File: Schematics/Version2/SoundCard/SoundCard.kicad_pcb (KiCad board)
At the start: 6 copper layers, 101.6 x 38.4 mm, 46 parts, among them J1 Screw_Terminal_01x03, J2 AudioJack3, J3 Conn, Q1 Q_NJFET_DSG, Q2 Q_NJFET_DSG, Q3 Q_NJFET_DSG, Q4 Q_NJFET_DSG, U1 TL072, U2 MAX505, U3 AS3340, U4 TL072, U5 TL072

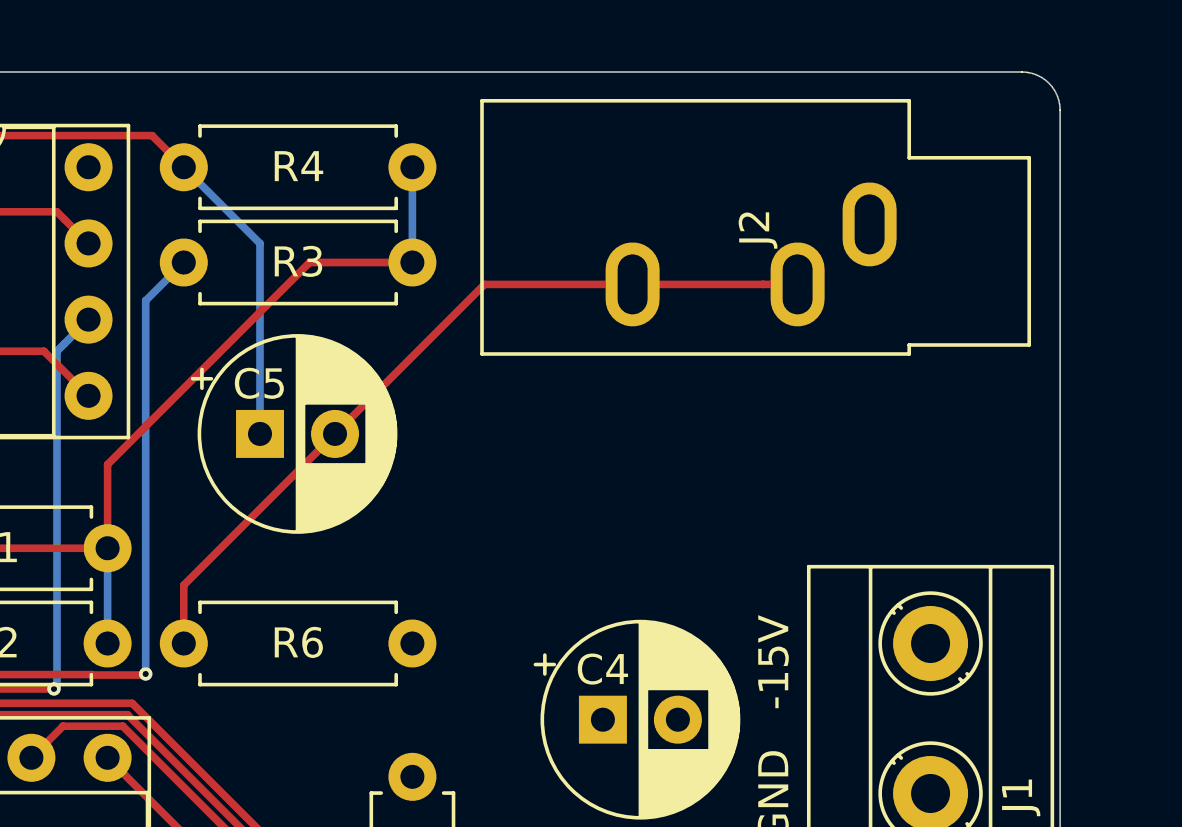
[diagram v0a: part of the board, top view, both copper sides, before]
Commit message: Update the footprint for the 3.5mm jack.
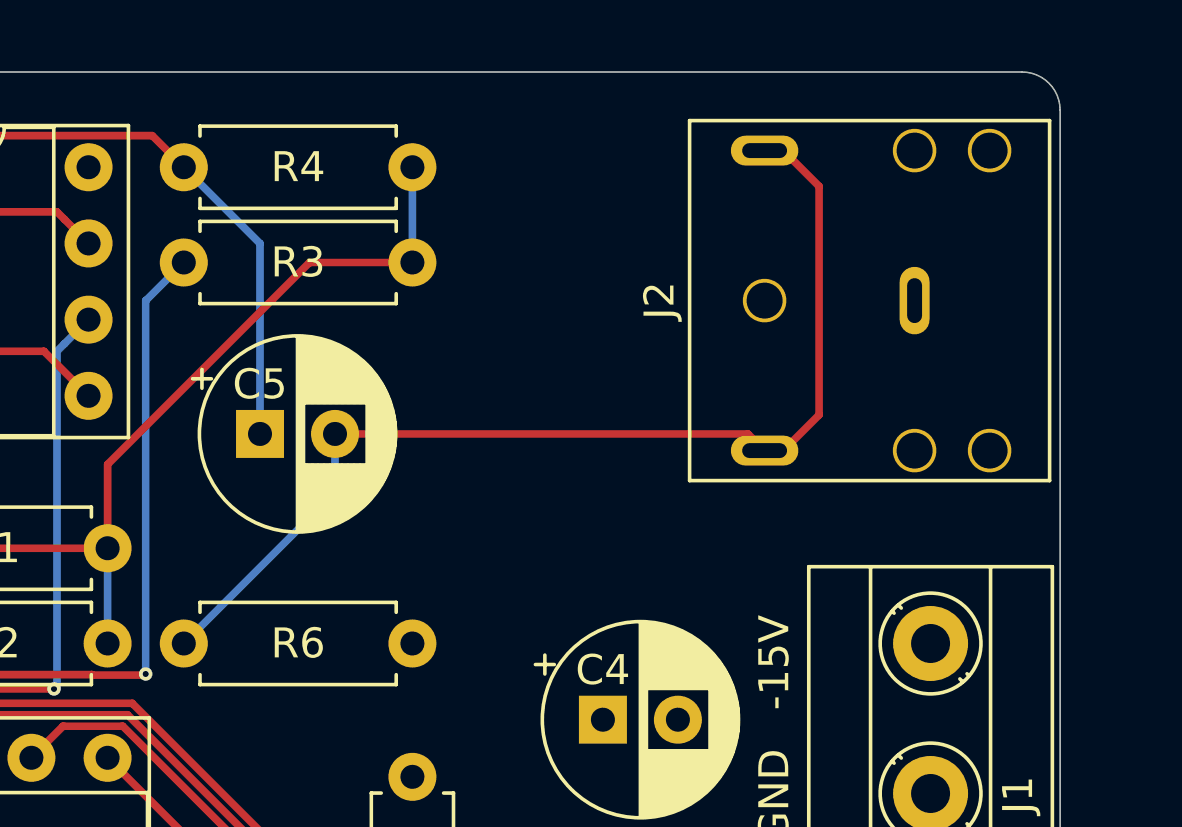
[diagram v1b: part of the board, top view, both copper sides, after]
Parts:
- J2: footprint Connector_Audio:Jack_3.5mm_CUI_SJ1-3533NG_Horizontal -> Connector_Audio:Jack_3.5mm_CUI_SJ1-3523N
- moved J2 2.54 mm to (158.8, 106.7)
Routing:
- net Net-(C5-Pad2): track 26.6 -> 35.9 mm
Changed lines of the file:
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@@
     (thickness 1.6)
     (drawings 11)
-    (tracks 297)
+    (tracks 300)
     (zones 0)
     (modules 46)
@@
     (add_net VCC)
   )
+  (module Connector_Audio:Jack_3.5mm_CUI_SJ1-3523N (layer F.Cu)
+    (at 158.75 106.68 270)
+    (fp_text reference J2 (at 0 7 270) (layer F.SilkS)
+      (effects (font (size 1 1) (thickness 0.15)))
+    )
+    (fp_text value AudioJack3 (at 0 8.5 270) (layer F.Fab)
+      (effects (font (size 1 1) (thickness 0.15)))
+    )
+    (fp_line (start -6 6) (end -6 -6) (layer F.SilkS) (width 0.12))
+    (fp_line (start 6 -6) (end 6 6) (layer F.SilkS) (width 0.12))
+    (fp_line (start -6 6) (end 6 6) (layer F.SilkS) (width 0.12))
+    (fp_line (start -6 -6) (end 6 -6) (layer F.SilkS) (width 0.12))
+    (pad "" thru_hole circle (at -5 -4) (size 1.45 1.45) (drill 1.2) (layers *.Cu *.Mask))
+    (pad "" thru_hole circle (at 5 -4) (size 1.45 1.45) (drill 1.2) (layers *.Cu *.Mask))
+    (pad "" thru_hole circle (at -5 -1.5) (size 1.45 1.45) (drill 1.2) (layers *.Cu *.Mask))
+    (pad "" thru_hole circle (at 5 -1.5) (size 1.45 1.45) (drill 1.2) (layers *.Cu *.Mask))
+    (pad "" thru_hole circle (at 0 3.5) (size 1.45 1.45) (drill 1.2) (layers *.Cu *.Mask))
+    (pad R thru_hole oval (at 5 3.5 270) (size 1 2.25) (drill oval 0.5 1.5) (layers *.Cu *.Mask)
+      (net 24 "Net-(C5-Pad2)"))
+    (pad T thru_hole oval (at -5 3.5 270) (size 1 2.25) (drill oval 0.5 1.5) (layers *.Cu *.Mask)
+      (net 24 "Net-(C5-Pad2)"))
+    (pad S thru_hole oval (at 0 -1.5) (size 1 2.25) (drill oval 0.5 1.5) (layers *.Cu *.Mask)
+      (net 23 GNDA))
+  )
   (module Connector_PinHeader_2.54mm:PinHeader_2x40_P2.54mm_Horizontal (layer F.Cu)
     (at 163.83 133.35 270)
@@
     )
   )
-  (module Connector_Audio:Jack_3.5mm_CUI_SJ1-3533NG_Horizontal (layer F.Cu)
-    (at 158.75 104.14 270)
-    (descr "TRS 3.5mm, horizontal, through-hole, https://www.cui.com/product/resource/sj1-353xng.pdf")
-    (tags "TRS audio jack stereo horizontal")
-    (fp_text reference J2 (at 0.1 3.81 270) (layer F.SilkS)
-      (effects (font (size 1 1) (thickness 0.15)))
-    )
-    (fp_text value AudioJack3 (at 0.1 14.05 270) (layer F.Fab)
-      (effects (font (size 1 1) (thickness 0.15)))
-    )
-    (fp_text user %R (at 0.1 3.8 270) (layer F.Fab)
-      (effects (font (size 1 1) (thickness 0.15)))
-    )
-    (fp_line (start 4.7 -5.7) (end -4.5 -5.7) (layer F.CrtYd) (width 0.05))
-    (fp_line (start 4.7 13.3) (end 4.7 -5.7) (layer F.CrtYd) (width 0.05))
-    (fp_line (start -4.5 13.3) (end 4.7 13.3) (layer F.CrtYd) (width 0.05))
-    (fp_line (start -4.5 -5.7) (end -4.5 13.3) (layer F.CrtYd) (width 0.05))
-    (fp_line (start -2.22 -1.32) (end -2.22 -5.32) (layer F.SilkS) (width 0.12))
-    (fp_line (start -4.12 -1.32) (end -2.22 -1.32) (layer F.SilkS) (width 0.12))
-    (fp_line (start -4.12 12.92) (end -4.12 -1.32) (layer F.SilkS) (width 0.12))
-    (fp_line (start 4.32 12.92) (end -4.12 12.92) (layer F.SilkS) (width 0.12))
-    (fp_line (start 4.32 -1.32) (end 4.32 12.92) (layer F.SilkS) (width 0.12))
-    (fp_line (start 4.02 -1.32) (end 4.32 -1.32) (layer F.SilkS) (width 0.12))
-    (fp_line (start 4.02 -5.32) (end 4.02 -1.32) (layer F.SilkS) (width 0.12))
-    (fp_line (start -2.22 -5.32) (end 4.02 -5.32) (layer F.SilkS) (width 0.12))
-    (fp_line (start -2.1 -1.2) (end -2.1 -5.2) (layer F.Fab) (width 0.1))
-    (fp_line (start -4 -1.2) (end -2.1 -1.2) (layer F.Fab) (width 0.1))
-    (fp_line (start -4 12.8) (end -4 -1.2) (layer F.Fab) (width 0.1))
-    (fp_line (start 4.2 12.8) (end -4 12.8) (layer F.Fab) (width 0.1))
-    (fp_line (start 4.2 -1.2) (end 4.2 12.8) (layer F.Fab) (width 0.1))
-    (fp_line (start 3.9 -1.2) (end 4.2 -1.2) (layer F.Fab) (width 0.1))
-    (fp_line (start 3.9 -5.2) (end 3.9 -1.2) (layer F.Fab) (width 0.1))
-    (fp_line (start -2.1 -5.2) (end 3.9 -5.2) (layer F.Fab) (width 0.1))
-    (pad R thru_hole oval (at 2 7.9 270) (size 2.8 1.8) (drill oval 2 1) (layers *.Cu *.Mask)
-      (net 24 "Net-(C5-Pad2)"))
-    (pad T thru_hole oval (at 2 2.4 270) (size 2.8 1.8) (drill oval 2 1) (layers *.Cu *.Mask)
-      (net 24 "Net-(C5-Pad2)"))
-    (pad S thru_hole oval (at 0 0 270) (size 2.8 1.8) (drill oval 2 1) (layers *.Cu *.Mask)
-      (net 23 GNDA))
-    (model ${KISYS3DMOD}/Connector_Audio.3dshapes/Jack_3.5mm_CUI_SJ1-3533NG_Horizontal.wrl
-      (at (xyz 0 0 0))
-      (scale (xyz 1 1 1))
-      (rotate (xyz 0 0 0))
-    )
-  )
   (module Capacitor_THT:CP_Radial_D6.3mm_P2.50mm (layer F.Cu)
     (at 149.86 120.65)
@@
   (segment (start 114.515999 125.945999) (end 117.310001 128.740001) (width 0.254) (layer B.Cu) (net 23))
   (segment (start 115.57 118.11) (end 114.515999 119.164001) (width 0.254) (layer B.Cu) (net 23))
-  (segment (start 155.196 106.14) (end 150.85 106.14) (width 0.254) (layer F.Cu) (net 24))
-  (segment (start 156.35 106.14) (end 155.196 106.14) (width 0.254) (layer F.Cu) (net 24))
-  (segment (start 145.915 106.14) (end 140.93 111.125) (width 0.254) (layer F.Cu) (net 24))
-  (segment (start 150.85 106.14) (end 145.915 106.14) (width 0.254) (layer F.Cu) (net 24))
-  (segment (start 135.89 116.165) (end 135.89 118.11) (width 0.254) (layer F.Cu) (net 24))
-  (segment (start 140.93 111.125) (end 135.89 116.165) (width 0.254) (layer F.Cu) (net 24))
+  (segment (start 140.93 113.07) (end 135.89 118.11) (width 0.254) (layer B.Cu) (net 24))
+  (segment (start 140.93 111.125) (end 140.93 113.07) (width 0.254) (layer B.Cu) (net 24))
+  (segment (start 154.695 111.125) (end 155.25 111.68) (width 0.254) (layer F.Cu) (net 24))
+  (segment (start 140.93 111.125) (end 154.695 111.125) (width 0.254) (layer F.Cu) (net 24))
+  (segment (start 155.875 101.68) (end 155.25 101.68) (width 0.254) (layer F.Cu) (net 24))
+  (segment (start 157.065 110.49) (end 157.065 102.87) (width 0.254) (layer F.Cu) (net 24))
+  (segment (start 155.875 111.68) (end 157.065 110.49) (width 0.254) (layer F.Cu) (net 24))
+  (segment (start 157.065 102.87) (end 155.875 101.68) (width 0.254) (layer F.Cu) (net 24))
+  (segment (start 155.25 111.68) (end 155.875 111.68) (width 0.254) (layer F.Cu) (net 24))
   (segment (start 126.149 102.235) (end 125.095 102.235) (width 0.254) (layer F.Cu) (net 25))
   (segment (start 134.835999 101.180999) (end 127.203001 101.180999) (width 0.254) (layer F.Cu) (net 25))

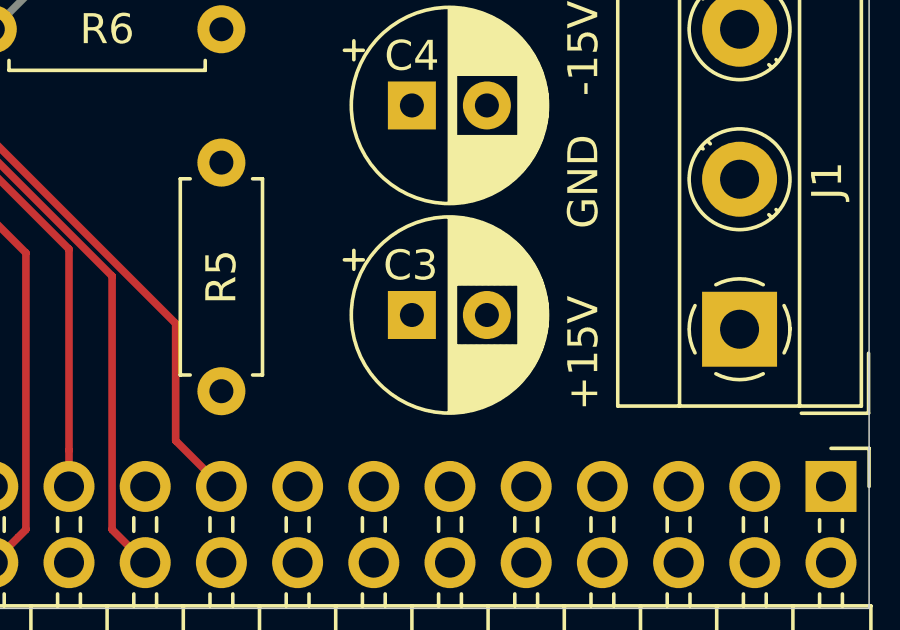
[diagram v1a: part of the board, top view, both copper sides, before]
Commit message: Rework the Sound Card PCB to use four layers instead of six.
One of the two inner copper layers is used for partially for the ground
plane and partially for the analog ground plane. The other inner layer is
used for VCC, +15V, and -15V, constructed of large copper fills over the
relevant areas.
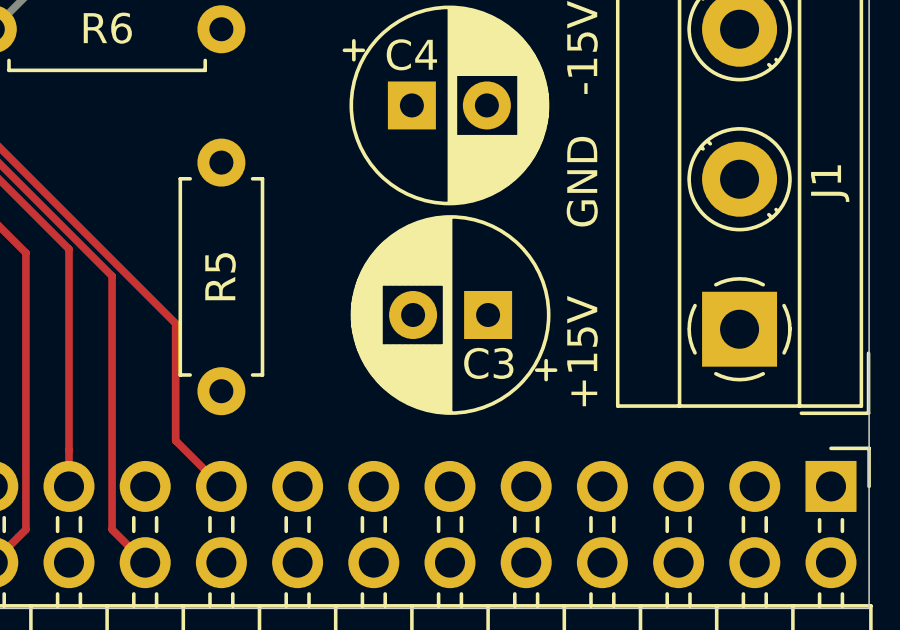
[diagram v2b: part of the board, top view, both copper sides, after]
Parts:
- moved C3 2.54 mm to (152.4, 127.6), turned to 180 degrees
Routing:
- net -15V: track 0.00 -> 127.1 mm
- added copper zone on In2.Cu, net -15V
- removed copper zone on In4.Cu, net -15V
- removed copper zone on In3.Cu, net GND
- removed copper zone on In4.Cu, net GND
- removed copper zone on In3.Cu, net GNDA
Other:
- copper layers 6 -> 4
